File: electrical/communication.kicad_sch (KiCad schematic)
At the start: 9 parts

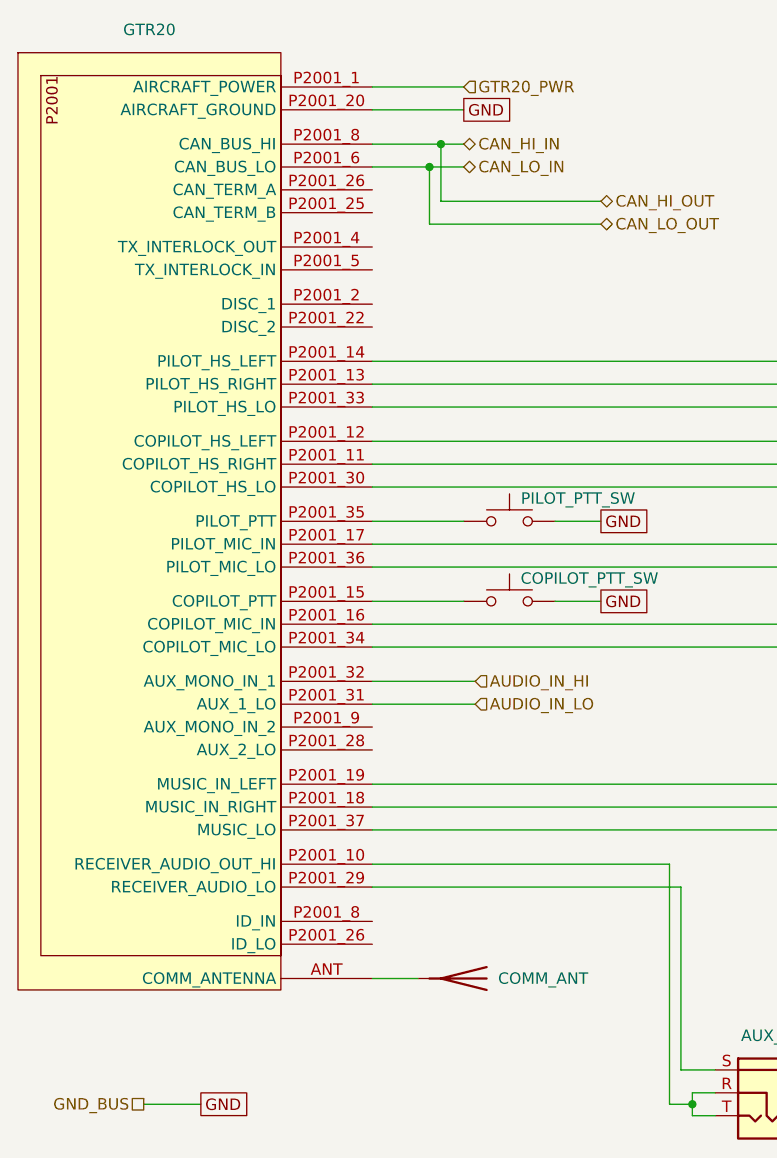
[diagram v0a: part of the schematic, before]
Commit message: Changed grounds and canbuses to be in/out when applicable.
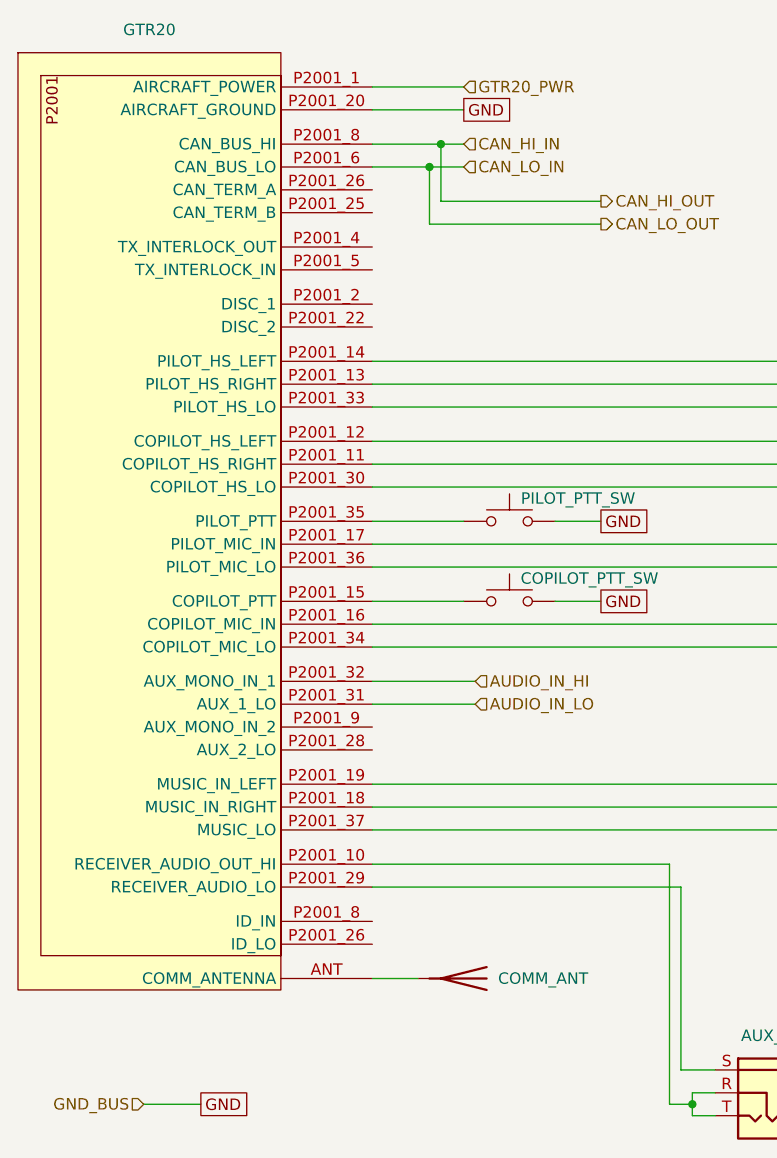
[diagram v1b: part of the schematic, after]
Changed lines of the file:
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@@
     )
   )
-  (hierarchical_label "CAN_LO_IN" (shape bidirectional) (at 83.82 46.99 0) (fields_autoplaced)
+  (hierarchical_label "CAN_LO_IN" (shape input) (at 83.82 46.99 0) (fields_autoplaced)
     (effects (font (size 1.27 1.27)) (justify left))
   )
@@
     (effects (font (size 1.27 1.27)) (justify left))
   )
-  (hierarchical_label "CAN_HI_IN" (shape bidirectional) (at 83.82 44.45 0) (fields_autoplaced)
+  (hierarchical_label "CAN_HI_IN" (shape input) (at 83.82 44.45 0) (fields_autoplaced)
     (effects (font (size 1.27 1.27)) (justify left))
   )
@@
     (effects (font (size 1.27 1.27)) (justify left))
   )
-  (hierarchical_label "CAN_HI_OUT" (shape bidirectional) (at 99.06 50.8 0) (fields_autoplaced)
+  (hierarchical_label "CAN_HI_OUT" (shape output) (at 99.06 50.8 0) (fields_autoplaced)
     (effects (font (size 1.27 1.27)) (justify left))
   )
@@
     (effects (font (size 1.27 1.27)) (justify left))
   )
-  (hierarchical_label "CAN_LO_OUT" (shape bidirectional) (at 99.06 53.34 0) (fields_autoplaced)
+  (hierarchical_label "CAN_LO_OUT" (shape output) (at 99.06 53.34 0) (fields_autoplaced)
     (effects (font (size 1.27 1.27)) (justify left))
   )
@@
     (effects (font (size 1.27 1.27)) (justify right))
   )
-  (hierarchical_label "GND_BUS" (shape passive) (at 48.26 151.13 180) (fields_autoplaced)
+  (hierarchical_label "GND_BUS" (shape input) (at 48.26 151.13 180) (fields_autoplaced)
     (effects (font (size 1.27 1.27)) (justify right))
   )
